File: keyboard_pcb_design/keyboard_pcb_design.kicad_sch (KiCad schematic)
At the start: 0 parts

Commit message: completed input supply schematic
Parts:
- added C1, C2: 10u, symbol Device:C
- added C3, C4: 1u, symbol Device:C
- added J1: USB_C_Receptacle_USB2.0_14P, symbol Connector:USB_C_Receptacle_USB2.0_14P
- added R1, R2: 5.1k, symbol Device:R
- added R3, R4: 27, symbol Device:R
- added U1: SC09147, keyboard_footprint:SC09147_QFN56_7X7_RPI, symbol keyboard_library:SC09147
- added U2: NCP1117-3.3_SOT223, Package_TO_SOT_SMD:SOT-223-3_TabPin2, symbol Regulator_Linear:NCP1117-3.3_SOT223
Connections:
- new net: J1.A5 (CC1), R1.2
- new net: J1.B5 (CC2), R2.2
- new net: R3.1, U1.47 (USB_DP)
- new net: R4.1, U1.46 (USB_DM)
- new net +1V1: C3.1, U1.23 (DVDD), U1.45 (VREG_VOUT), U1.50 (DVDD)
- new net +3V3: C2.1, C4.1, U1.1 (IOVDD), U1.10 (IOVDD), U1.33 (IOVDD), U1.42 (IOVDD), U1.43 (ADC_AVDD), U1.44 (VREG_VIN), U1.48 (USB_VDD), U1.49 (IOVDD), U2.2 (VO)
- new net GND: C1.2, C2.2, C3.2, C4.2, J1.A1 (GND), J1.A12 (GND), J1.B1 (GND), J1.B12 (GND), J1.S1 (SHIELD), R1.1, R2.1, U1.57 (GND), U2.1 (GND)
- new net USB_D+: J1.A6 (D+), J1.B6 (D+), R3.2
- new net USB_D-: J1.A7 (D-), J1.B7 (D-), R4.2
- new net VBUS: C1.1, J1.A4 (VBUS), J1.A9 (VBUS), J1.B4 (VBUS), J1.B9 (VBUS), U2.3 (VI)
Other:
- note added: "power"

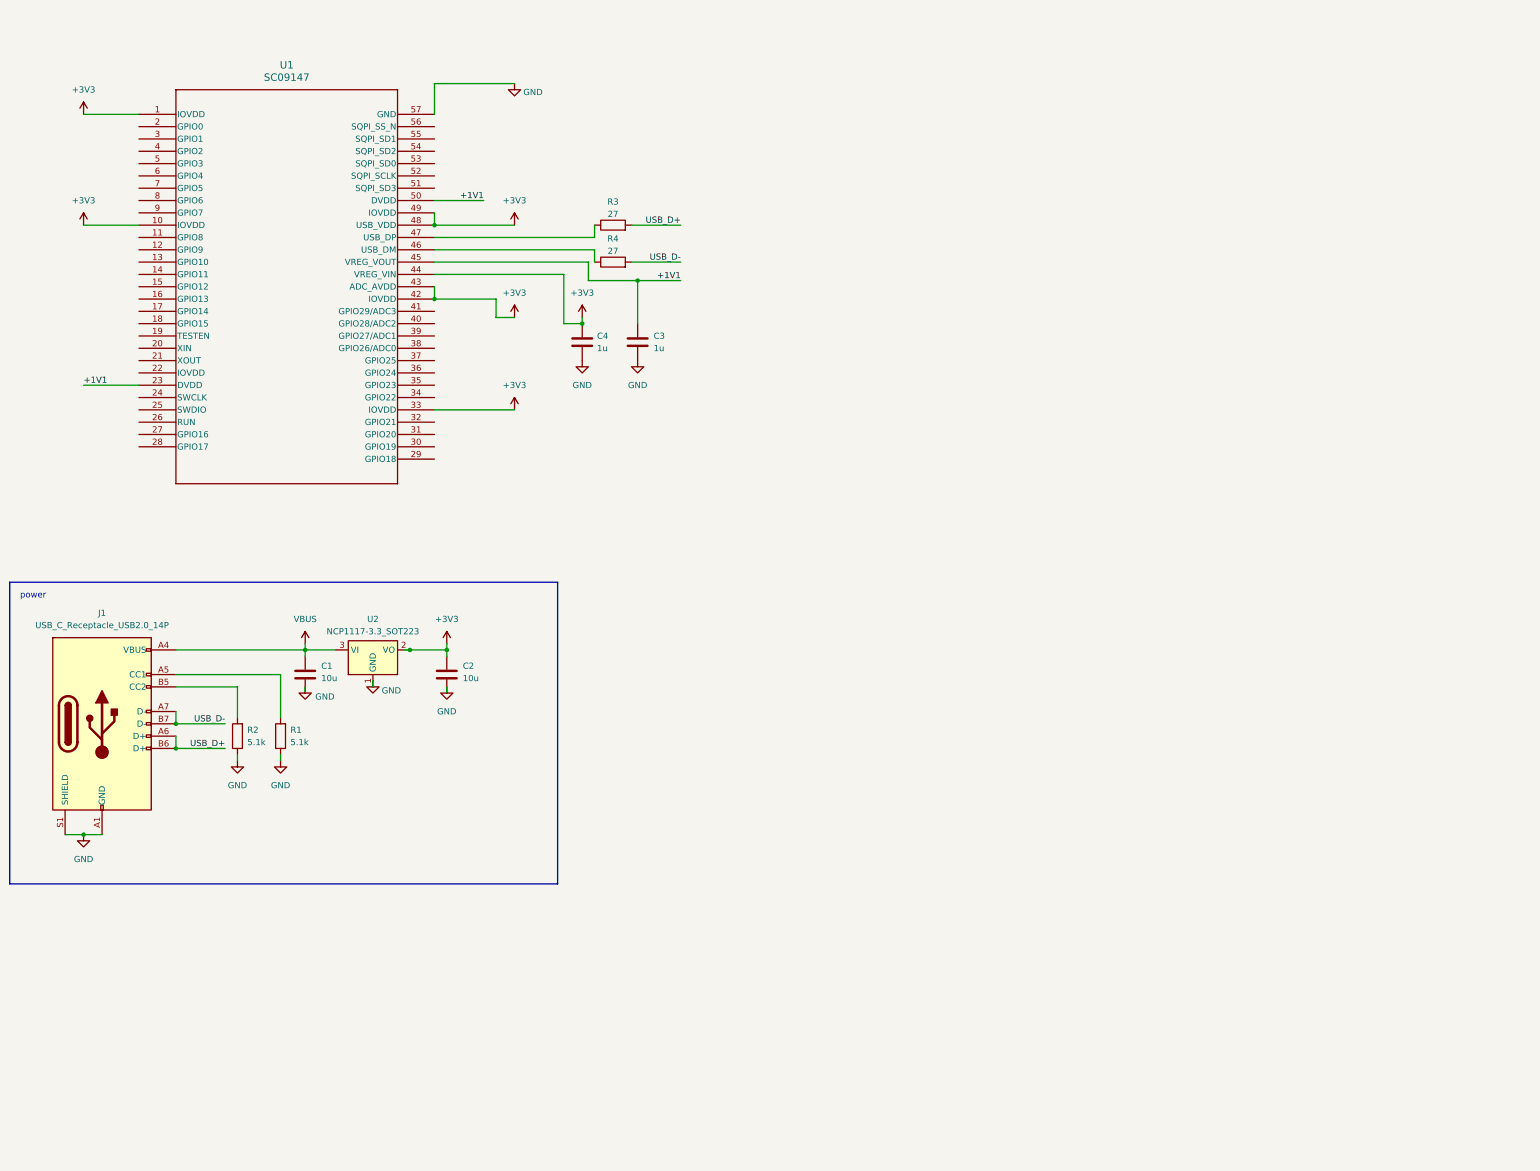
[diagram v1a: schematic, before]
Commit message: completed decoupling capacitors schematics
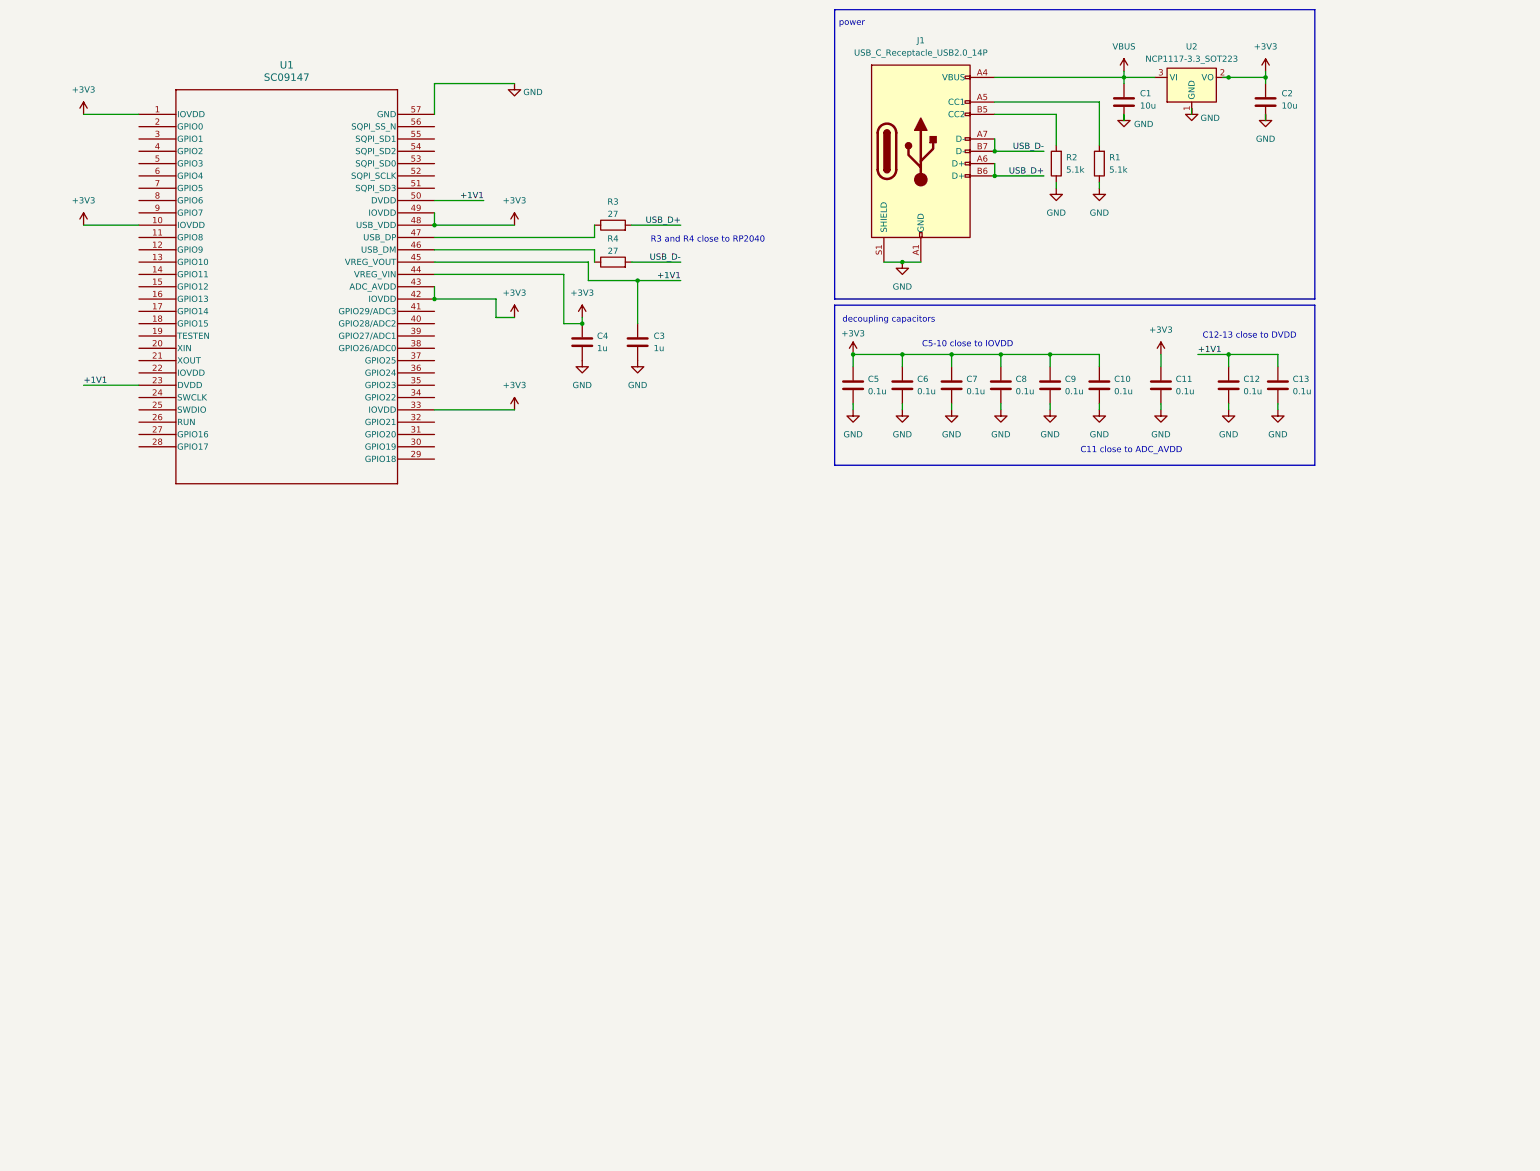
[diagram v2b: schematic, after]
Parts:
- added C10, C11, C12, C13, C5, C6, C7, C8, C9: 0.1u, symbol Device:C
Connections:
- net +1V1: now also C12.1, C13.1
- net +3V3: now also C10.1, C11.1, C5.1, C6.1, C7.1, C8.1, C9.1
- net GND: now also C10.2, C11.2, C12.2, C13.2, C5.2, C6.2, C7.2, C8.2, C9.2
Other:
- note added: "C11 close to ADC_AVDD"
- note added: "C12-13 close to DVDD"
- note added: "C5-10 close to IOVDD"
- note added: "R3 and R4 close to RP2040"
- note added: "decoupling capacitors"
- moved on the sheet: C1, C2, J1, R1, R2, U2

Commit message: saved crystal oscillator schematic
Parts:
- added C14, C15: 15p, symbol Device:C
- added R5: 1k, symbol Device:R
- added X1: ABM8-272-T3, keyboard_footprint:XTAL_ABM8-272-T3, symbol keyboard_library:ABM8-272-T3
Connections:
- net GND: now also C14.2, C15.1, X1.2, X1.4
- net XIN: now reaches U1.20 (XIN)
- net XIN: now also C14.1, X1.1
- net XOUT: now reaches U1.21 (XOUT)
- net XOUT: now also R5.1
- new net: C15.2, R5.2, X1.3
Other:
- note added: "crystal oscillator"
- moved on the sheet: C1, C10, C11, C12, C13, C2, C5, C6, C7, C8, C9, J1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

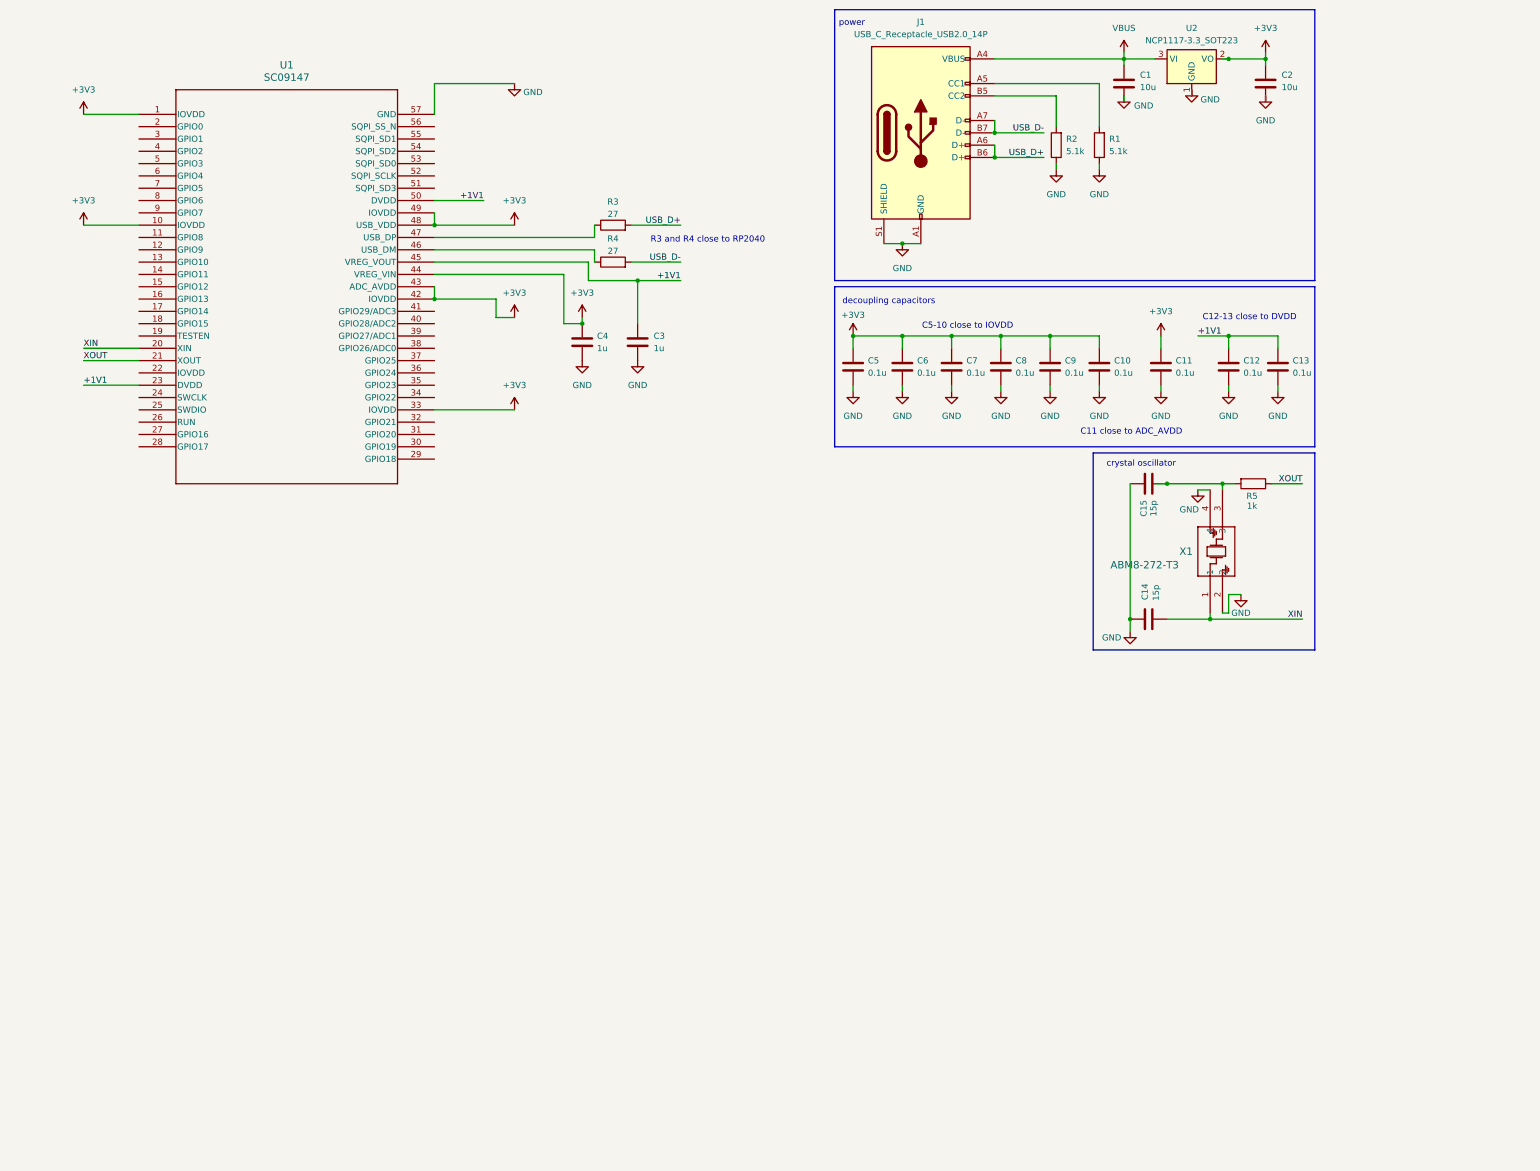
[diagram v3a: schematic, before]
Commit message: flash storage schematic wip
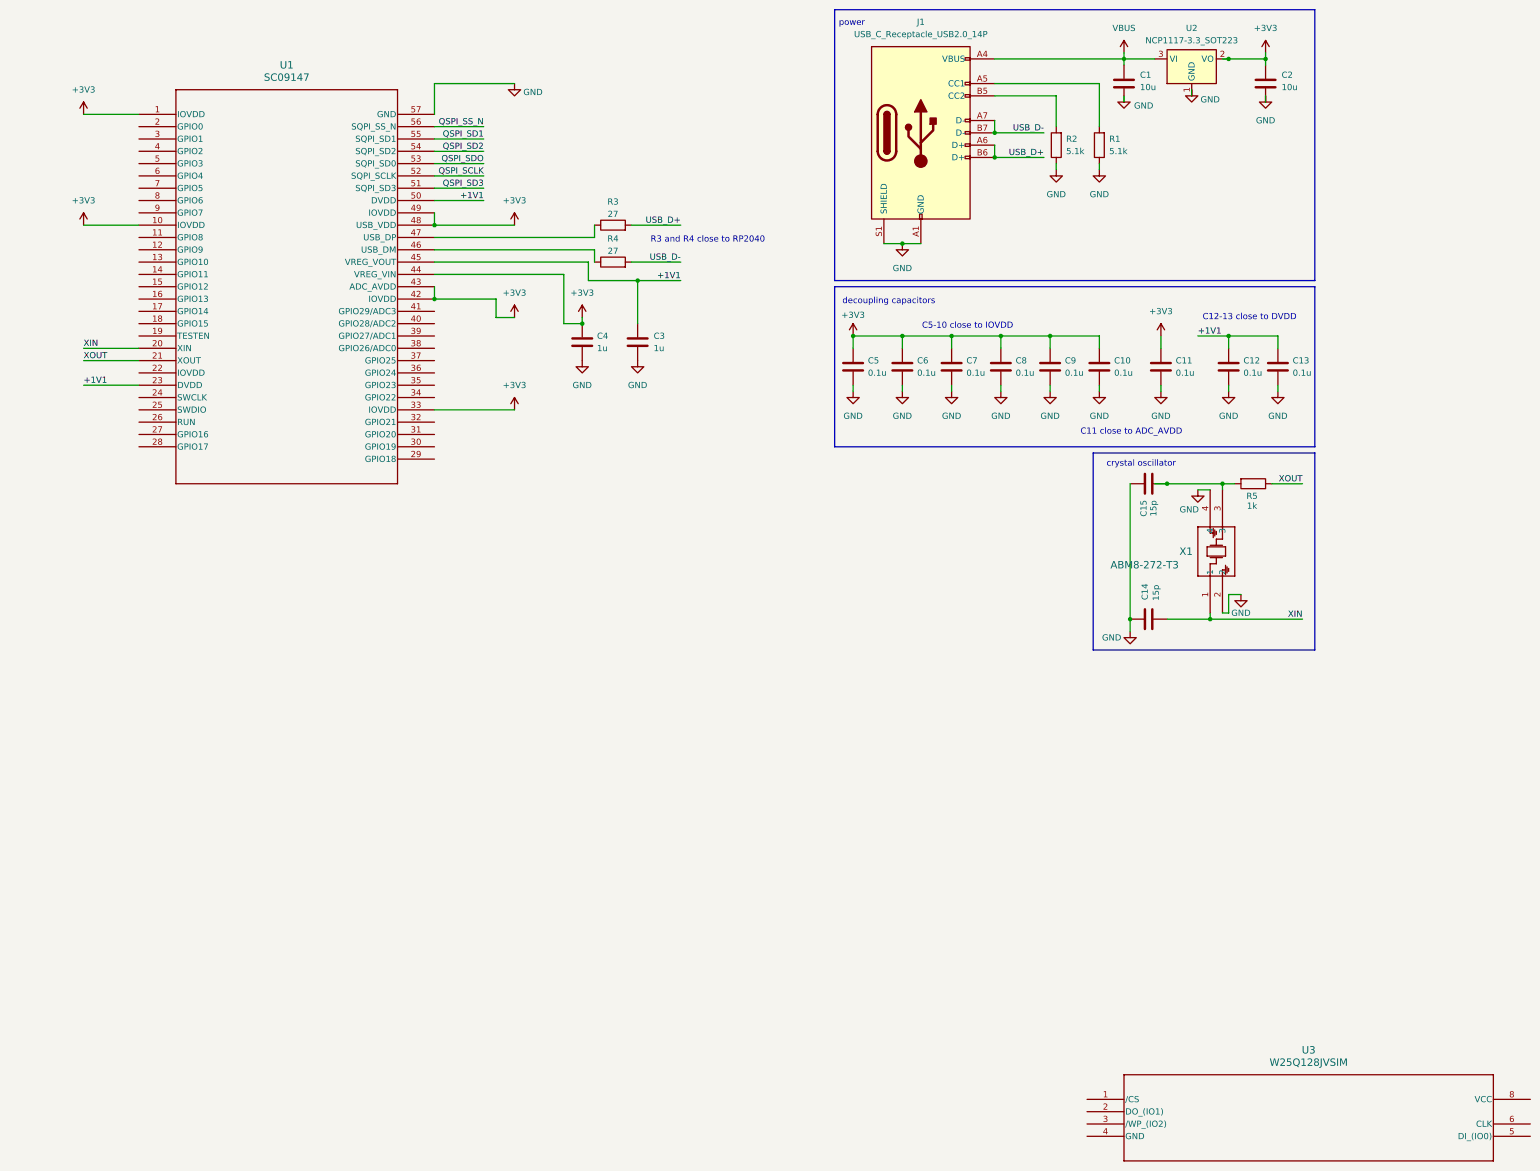
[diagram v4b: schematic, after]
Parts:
- added U3: W25Q128JVSIM, keyboard_footprint:SOIC_128JVSIM_WIN, symbol keyboard_library:W25Q128JVSIM
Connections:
- net QSPI_SD3: now reaches U1.51 (SQPI_SD3)
- net QSPI_SCLK: now reaches U1.52 (SQPI_SCLK)
- net QSPI_SDO: now reaches U1.53 (SQPI_SD0)
- net QSPI_SD2: now reaches U1.54 (SQPI_SD2)
- net QSPI_SD1: now reaches U1.55 (SQPI_SD1)
- net QSPI_SS_N: now reaches U1.56 (SQPI_SS_N)
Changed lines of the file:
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@@
 	(wire
 		(pts
+			(xy 113.03 46.99) (xy 102.87 46.99)
+		)
+		(stroke
+			(width 0)
+			(type default)
+		)
+	)
+	(wire
+		(pts
 			(xy 113.03 52.07) (xy 102.87 52.07)
 		)
@@
 	(wire
 		(pts
+			(xy 113.03 36.83) (xy 102.87 36.83)
+		)
+		(stroke
+			(width 0)
+			(type default)
+		)
+	)
+	(wire
+		(pts
 			(xy 218.44 40.64) (xy 218.44 43.18)
 		)
@@
 	(wire
 		(pts
+			(xy 113.03 41.91) (xy 102.87 41.91)
+		)
+		(stroke
+			(width 0)
+			(type default)
+		)
+	)
+	(wire
+		(pts
 			(xy 189.23 91.44) (xy 189.23 90.17)
 		)
@@
 	(wire
 		(pts
+			(xy 113.03 39.37) (xy 102.87 39.37)
+		)
+		(stroke
+			(width 0)
+			(type default)
+		)
+	)
+	(wire
+		(pts
 			(xy 102.87 59.69) (xy 135.89 59.69)
 		)
@@
 	(wire
 		(pts
+			(xy 113.03 44.45) (xy 102.87 44.45)
+		)
+		(stroke
+			(width 0)
+			(type default)
+		)
+	)
+	(wire
+		(pts
 			(xy 259.08 29.21) (xy 259.08 30.48)
 		)
@@
 	(wire
 		(pts
+			(xy 113.03 49.53) (xy 102.87 49.53)
+		)
+		(stroke
+			(width 0)
+			(type default)
+		)
+	)
+	(wire
+		(pts
 			(xy 254 138.43) (xy 262.89 138.43)
 		)
@@
 		)
 	)
+	(label "QSPI_SD3"
+		(at 113.03 49.53 180)
+		(effects
+			(font
+				(size 1.27 1.27)
+			)
+			(justify right bottom)
+		)
+	)
 	(label "+1V1"
 		(at 30.48 90.17 0)
@@
 		)
 	)
+	(label "QSPI_SD1"
+		(at 113.03 39.37 180)
+		(effects
+			(font
+				(size 1.27 1.27)
+			)
+			(justify right bottom)
+		)
+	)
 	(label "+1V1"
 		(at 260.35 80.01 0)
@@
 		)
 	)
+	(label "QSPI_SS_N"
+		(at 113.03 36.83 180)
+		(effects
+			(font
+				(size 1.27 1.27)
+			)
+			(justify right bottom)
+		)
+	)
 	(label "+1V1"
 		(at 113.03 52.07 180)
@@
 		)
 	)
+	(label "QSPI_SCLK"
+		(at 113.03 46.99 180)
+		(effects
+			(font
+				(size 1.27 1.27)
+			)
+			(justify right bottom)
+		)
+	)
+	(label "QSPI_SD2"
+		(at 113.03 41.91 180)
+		(effects
+			(font
+				(size 1.27 1.27)
+			)
+			(justify right bottom)
+		)
+	)
 	(label "XOUT"
 		(at 281.94 110.49 180)
@@
 		)
 	)
+	(label "QSPI_SDO"
+		(at 113.03 44.45 180)
+		(effects
+			(font
+				(size 1.27 1.27)
+			)
+			(justify right bottom)
+		)
+	)
 	(label "USB_D-"
 		(at 228.6 38.1 180)
@@
 					(unit 1)
 				)
+			)
+		)
+	)
+	(symbol
+		(lib_id "keyboard_library:W25Q128JVSIM")
+		(at 237.49 237.49 0)
+		(unit 1)
+		(exclude_from_sim no)
+		(in_bom yes)
+		(on_board yes)
+		(dnp no)
+		(fields_autoplaced yes)
+		(property "Reference" "U3"
+			(at 283.21 227.33 0)
+			(effects
+				(font
+					(size 1.524 1.524)
+				)
+			)
+		)
+		(property "Value" "W25Q128JVSIM"
+			(at 283.21 229.87 0)
+			(effects
+				(font
+					(size 1.524 1.524)
+				)
+			)
+		)
+		(property "Footprint" "keyboard_footprint:SOIC_128JVSIM_WIN"
+			(at 237.49 237.49 0)
+			(effects
+				(font
+					(size 1.27 1.27)
+					(italic yes)
+				)
+				(hide yes)
+			)
+		)
+		(property "Datasheet" "W25Q128JVSIM"
+			(at 237.49 237.49 0)
+			(effects
+				(font
+					(size 1.27 1.27)
+					(italic yes)
+				)
+				(hide yes)
+			)
+		)
+		(property "Description" ""
+			(at 237.49 237.49 0)
+			(effects
+				(font
+					(size 1.27 1.27)
+				)
+				(hide yes)
+			)
+		)
+		(pin "5"
+		)
+		(pin "4"
+		)
+		(pin "3"
+		)
+		(pin "2"
+		)
+		(pin "6"
+		)
+		(pin "1"
+		)
+		(pin "8"
+		)
+		(instances
+			(project ""
+				(path "/f9810ab7-9213-4203-bfa9-6536d5a4d26a"
+					(reference "U3")
+					(unit 1)
+				)

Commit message: completed qspi flash storage schematic
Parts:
- removed U3: W25Q128JVSIM, keyboard_footprint:SOIC_128JVSIM_WIN, symbol keyboard_library:W25Q128JVSIM
- added C16: 0.1u, symbol Device:C
- added R6: 1k, symbol Device:R
- added R7: 10k, symbol Device:R
- added U3: MX25L3233FM2I-08Q, symbol keyboard_library:MX25L3233FM2I-08Q
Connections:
- net +3V3: now also C16.1, R7.1, U3.8 (VCC)
- net GND: now also C16.2, U3.4 (GND)
- net QSPI_SD1: now also U3.2 (SO/SIO1)
- net QSPI_SD2: now also U3.3 (~{WP}/SIO2)
- net QSPI_SD3: now also U3.7 (~{HOLD}/SIO3)
- net QSPI_SDO: now also U3.5 (SI/SIO0)
- net QSPI_SCLK renamed QSPI_SCK
- net QSPI_SCK: now also U3.6 (SCLK)
- net QSPI_SS_N renamed QSPI_CS
- net QSPI_CS: now also R6.1, R7.2, U3.1 (~{CS})
- new net USB_BOOT: R6.2
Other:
- note added: "qspi flash"
- moved on the sheet: C14, C15, R5, X1
